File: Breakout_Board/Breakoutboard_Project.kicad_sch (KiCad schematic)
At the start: 9 parts, among them U2 STM32F411

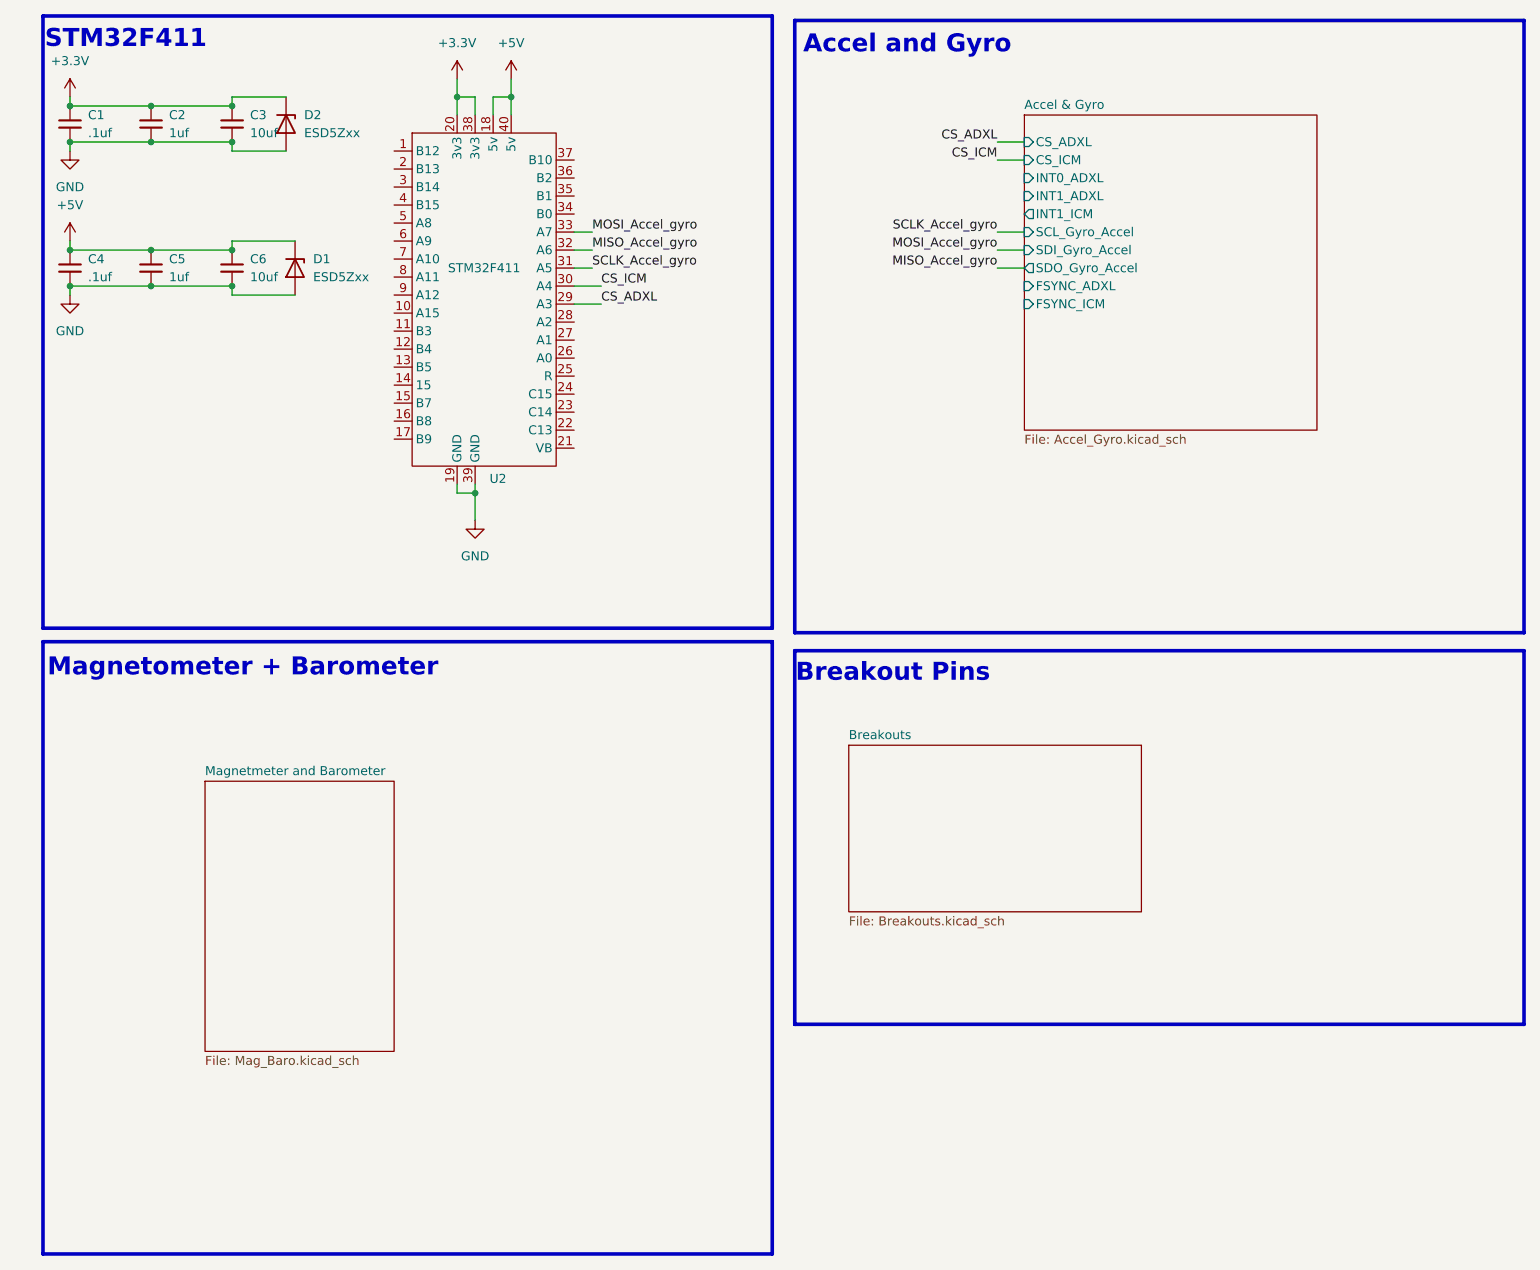
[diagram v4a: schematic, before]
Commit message: completed mag and baromet
fInished mag and barometer connections and connected to stm32f411, I just need the breakout pins to be done now.
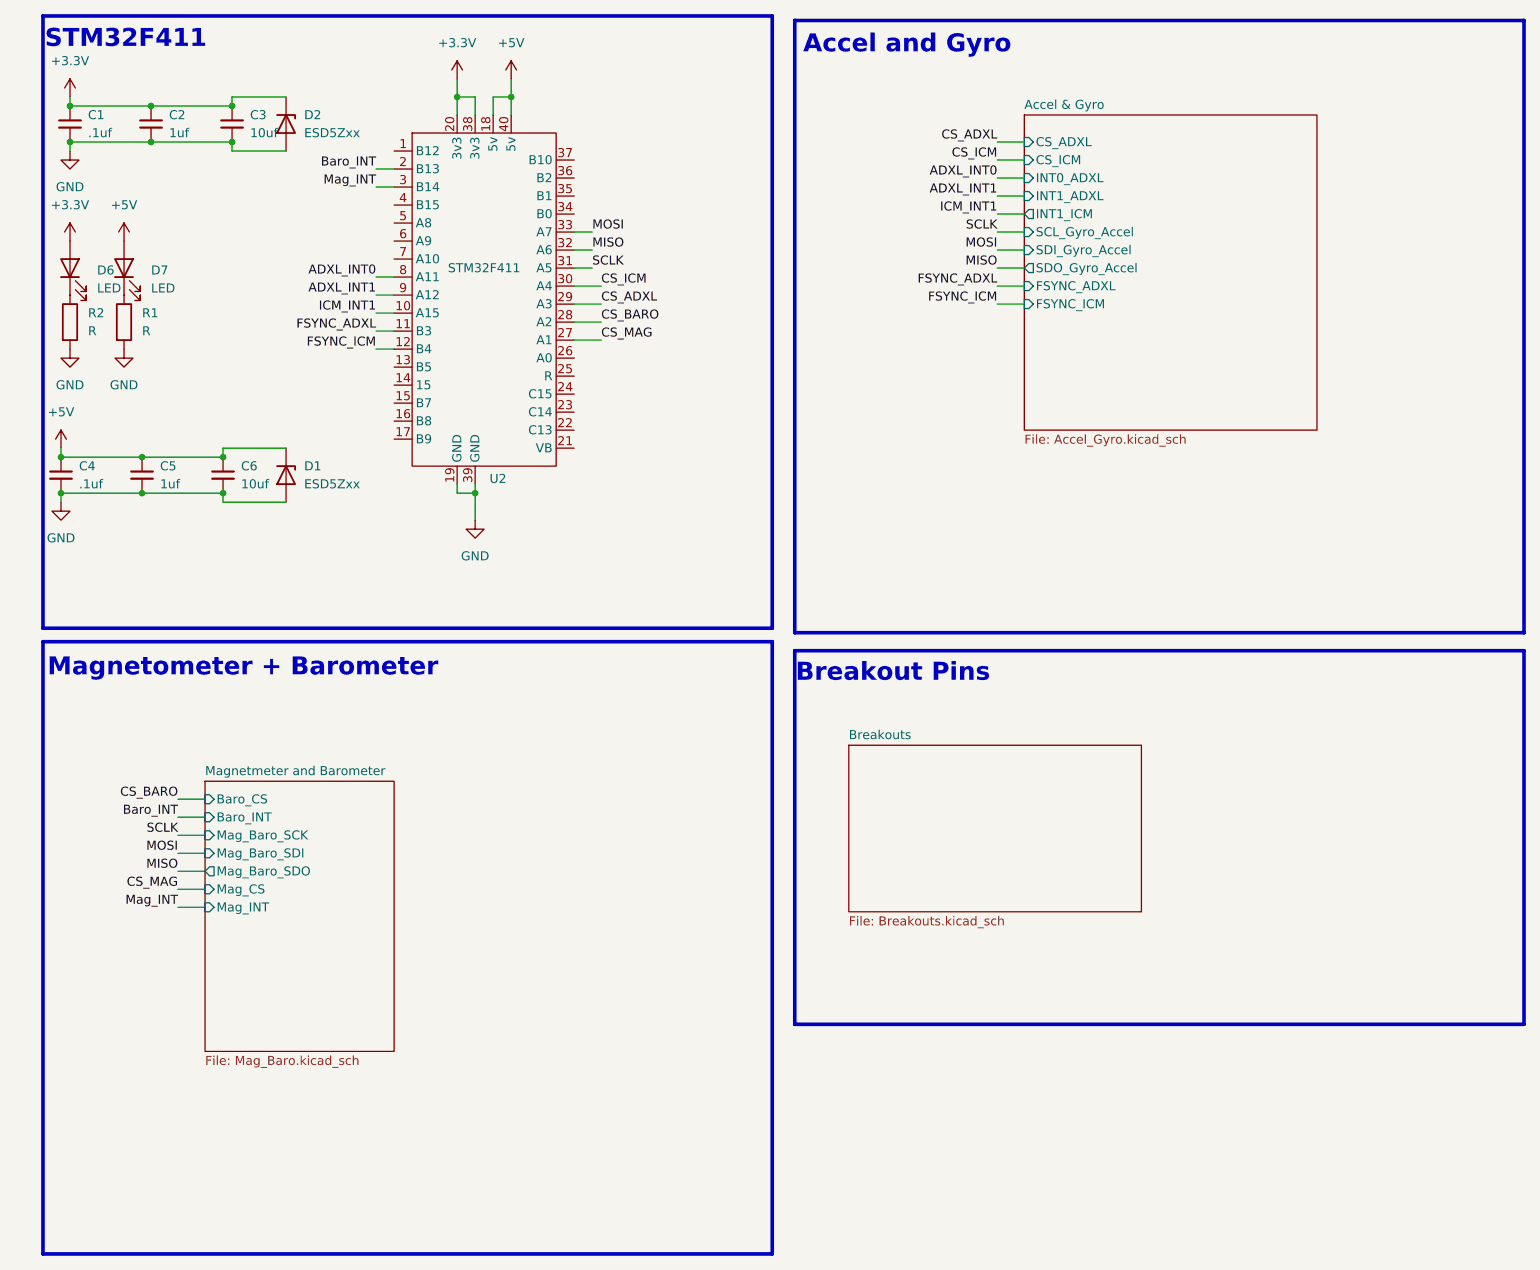
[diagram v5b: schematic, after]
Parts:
- added D6, D7: LED, LED_SMD:LED_0805_2012Metric_Pad1.15x1.40mm_HandSolder, symbol Device:LED
- added R1, R2: R, LED_SMD:LED_0805_2012Metric_Pad1.15x1.40mm_HandSolder, symbol Device:R
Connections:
- net +3.3V: now also D6.2 (A)
- net +5V: now also D7.2 (A)
- net GND: now also R1.2, R2.2
- net ICM_INT1: now reaches U2.10 (A15)
- net FSYNC_ADXL: now reaches U2.11 (B3)
- net FSYNC_ICM: now reaches U2.12 (B4)
- net Baro_INT: now reaches U2.2 (B13)
- net CS_MAG: now reaches U2.27 (A1)
- net CS_BARO: now reaches U2.28 (A2)
- net Mag_INT: now reaches U2.3 (B14)
- net ADXL_INT0: now reaches U2.8 (A11)
- net ADXL_INT1: now reaches U2.9 (A12)
- net MISO_Accel_gyro renamed MISO
- net MOSI_Accel_gyro renamed MOSI
- net SCLK_Accel_gyro renamed SCLK
- new net: D7.1 (K), R1.1
- new net: D6.1 (K), R2.1
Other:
- sheet Magnetmeter and Barometer ports: added Baro_CS, Baro_INT, Mag_Baro_SCK, Mag_Baro_SDI, Mag_Baro_SDO, Mag_CS, Mag_INT; removed none
- moved on the sheet: C4, C5, C6, D1

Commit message: ready for breakout
Fixed up some work, now its ready for breakouts before final PCB layout
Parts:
- added J1: Conn_01x17, Package_QFP:LQFP-176_24x24mm_P0.5mm, symbol Connector_Generic:Conn_01x17
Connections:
- net B12: now reaches U2.1 (B12)
- net B5: now reaches U2.13 (B5)
- net B6: now reaches U2.14 (B6)
- net B7: now reaches U2.15 (B7)
- net B8: now reaches U2.16 (B8)
- net B9: now reaches U2.17 (B9)
- net VB: now reaches U2.21 (VB)
- net C13: now reaches U2.22 (C13)
- net C14: now reaches U2.23 (C14)
- net C15: now reaches U2.24 (C15)
- net R: now reaches U2.25 (R)
- net A0: now reaches U2.26 (A0)
- net B0: now reaches U2.34 (B0)
- net B1: now reaches U2.35 (B1)
- net B2: now reaches U2.36 (B2)
- net B10: now reaches U2.37 (B10)
- net B15: now reaches U2.4 (B15)
- net A8: now reaches U2.5 (A8)
- net A9: now reaches U2.6 (A9)
- net A10: now reaches U2.7 (A10)
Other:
- removed sheet Breakouts
